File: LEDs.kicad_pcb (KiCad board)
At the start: 2 copper layers, 88.9 x 61.6 mm, 102 parts, among them J1 USB C, J2 UART, J3 LEDs, Q1 G30N03D3, Q10 SI2303, Q11 BSS138, Q12 BSS138, Q13 BSS138, Q2 G30N03D3, Q3 BSS138, Q4 BSS138, Q5 SI2303, Q6 BSS138, Q7 BSS138, Q8 AO4407C, Q9 BSS138, SW1 4-pin, U1 TP4056, U2 DW01A, U3 MT3608, U4 MT3608, U5 ESP32-C3-WROOM-02, U6 AMS1117-3.3, U7 DS18B20, U8 LM358S, U9 TUSB321

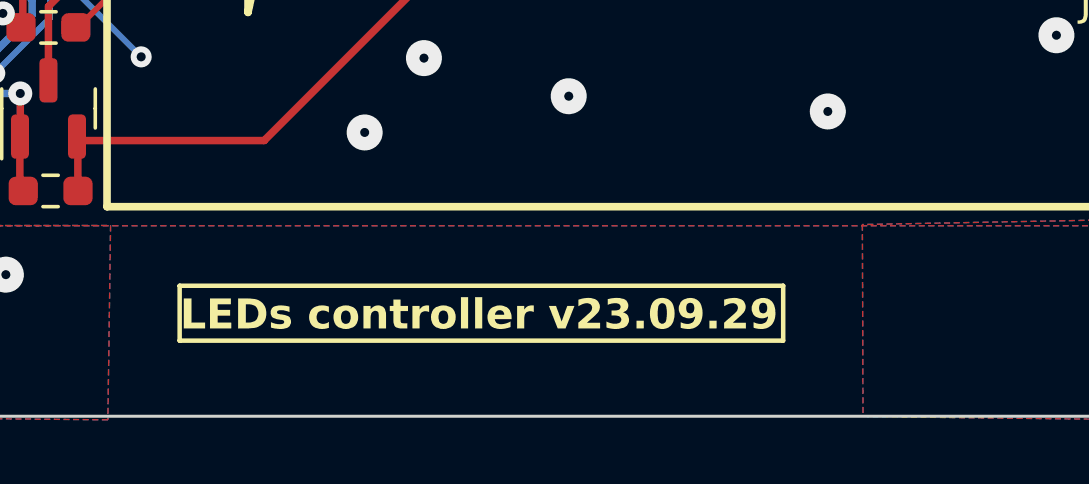
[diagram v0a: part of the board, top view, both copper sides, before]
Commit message: Rename board ver, add photos
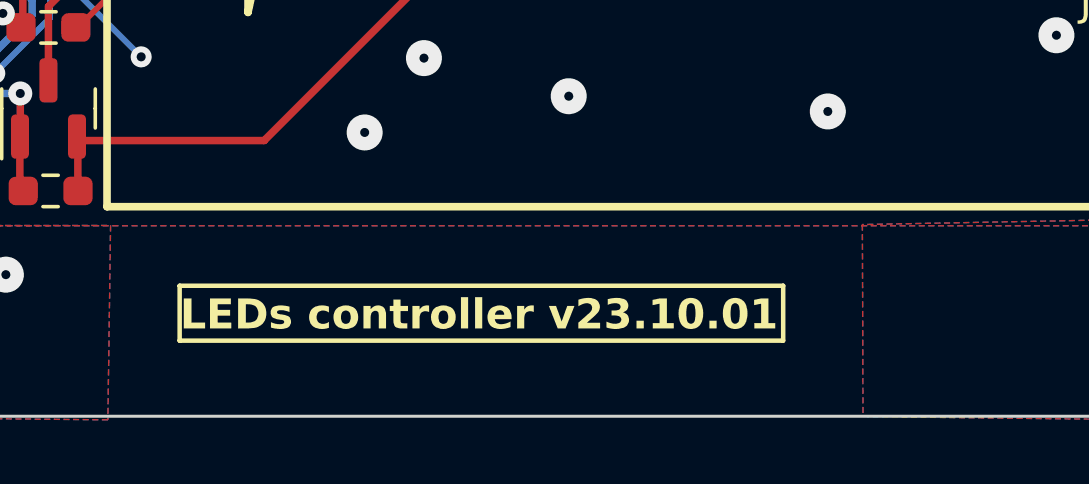
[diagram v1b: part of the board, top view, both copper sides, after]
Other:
- board text added: "LEDs controller v23.10.01"
- board text removed: "LEDs controller v23.09.29"
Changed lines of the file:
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@@
     (effects (font (size 1 1) (thickness 0.15)) (justify left bottom))
   )
-  (gr_text "LEDs controller v23.09.29\n\n\n" (at 72.894 131.57) (layer "F.SilkS" knockout)
+  (gr_text "LEDs controller v23.10.01\n\n\n" (at 72.894 131.57) (layer "F.SilkS" knockout)
     (effects (font (size 1 1) (thickness 0.2) bold) (justify left))
   )

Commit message: Small resistor change
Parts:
- R12, R14: value 90.9 -> 100
- R27: value 4.7k -> 5.1k
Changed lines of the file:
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@@
     (descr "Resistor SMD 0603 (1608 Metric), square (rectangular) end terminal, IPC_7351 nominal with elongated pad for handsoldering. (Body size source: IPC-SM-782 page 72, https://www.pcb-3d.com/wordpress/wp-content/uploads/ipc-sm-782a_amendment_1_and_2.pdf), generated with kicad-footprint-generator")
     (tags "resistor handsolder")
-    (property "LCSC" "C101232")
+    (property "LCSC" "C3017758")
     (property "Sheetfile" "LEDs.kicad_sch")
     (property "Sheetname" "")
@@
         (effects (font (size 1 1) (thickness 0.15)))
     )
-    (fp_text value "90.9" (at 0 1.43) (layer "F.Fab")
+    (fp_text value "100" (at 0 1.43) (layer "F.Fab")
         (effects (font (size 1 1) (thickness 0.15)))
     )
@@
     (descr "ESP32-C3-WROOM-02: https://www.espressif.com/sites/default/files/documentation/esp32-c3-wroom-02_datasheet_en.pdf")
     (tags "ESP32-C3")
-    (property "LCSC" "C2934560")
+    (property "LCSC" "C2944070")
     (property "Sheetfile" "LEDs.kicad_sch")
     (property "Sheetname" "")
@@
     (descr "Resistor SMD 0603 (1608 Metric), square (rectangular) end terminal, IPC_7351 nominal with elongated pad for handsoldering. (Body size source: IPC-SM-782 page 72, https://www.pcb-3d.com/wordpress/wp-content/uploads/ipc-sm-782a_amendment_1_and_2.pdf), generated with kicad-footprint-generator")
     (tags "resistor handsolder")
-    (property "LCSC" "C101232")
+    (property "LCSC" "C3017758")
     (property "Sheetfile" "LEDs.kicad_sch")
     (property "Sheetname" "")
@@
         (effects (font (size 1 1) (thickness 0.15)))
     )
-    (fp_text value "90.9" (at 0 1.43) (layer "F.Fab")
+    (fp_text value "100" (at 0 1.43) (layer "F.Fab")
         (effects (font (size 1 1) (thickness 0.15)))
     )
@@
     (descr "Resistor SMD 0603 (1608 Metric), square (rectangular) end terminal, IPC_7351 nominal with elongated pad for handsoldering. (Body size source: IPC-SM-782 page 72, https://www.pcb-3d.com/wordpress/wp-content/uploads/ipc-sm-782a_amendment_1_and_2.pdf), generated with kicad-footprint-generator")
     (tags "resistor handsolder")
-    (property "LCSC" "C3017722")
+    (property "LCSC" "C2907114")
     (property "Sheetfile" "LEDs.kicad_sch")
     (property "Sheetname" "")
@@
         (effects (font (size 1 1) (thickness 0.15)))
     )
-    (fp_text value "4.7k" (at 0 1.43) (layer "F.Fab")
+    (fp_text value "5.1k" (at 0 1.43) (layer "F.Fab")
         (effects (font (size 1 1) (thickness 0.15)))
     )
